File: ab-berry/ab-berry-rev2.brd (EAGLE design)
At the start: 58.4 x 61 mm, 72 parts, among them IC1 STM32F303CCT6, IC2 AT45DB161D-SU, U1 LM1117MPX-3.3/NOPB or AP2114H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, U2 PRTR5V0U2X

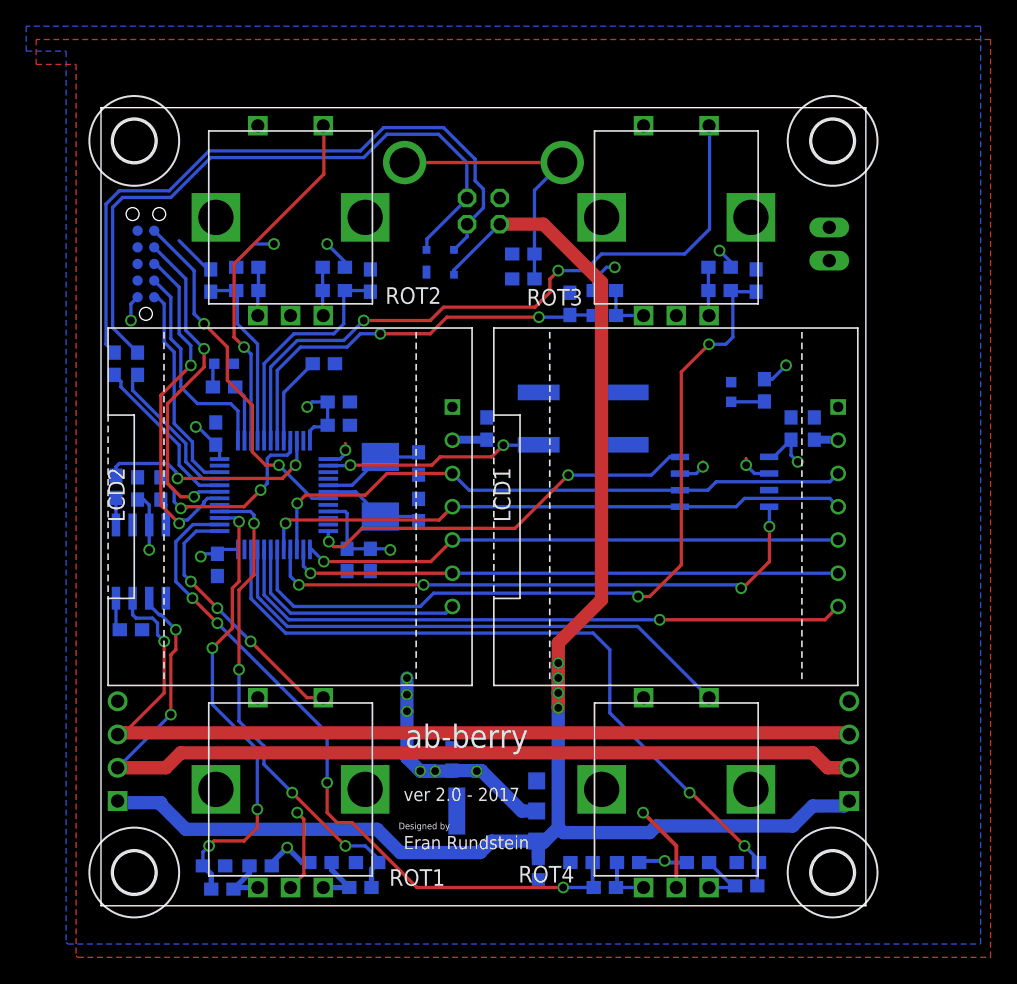
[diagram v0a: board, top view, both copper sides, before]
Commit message: make ab-berry-rev2 pass oshpask drc
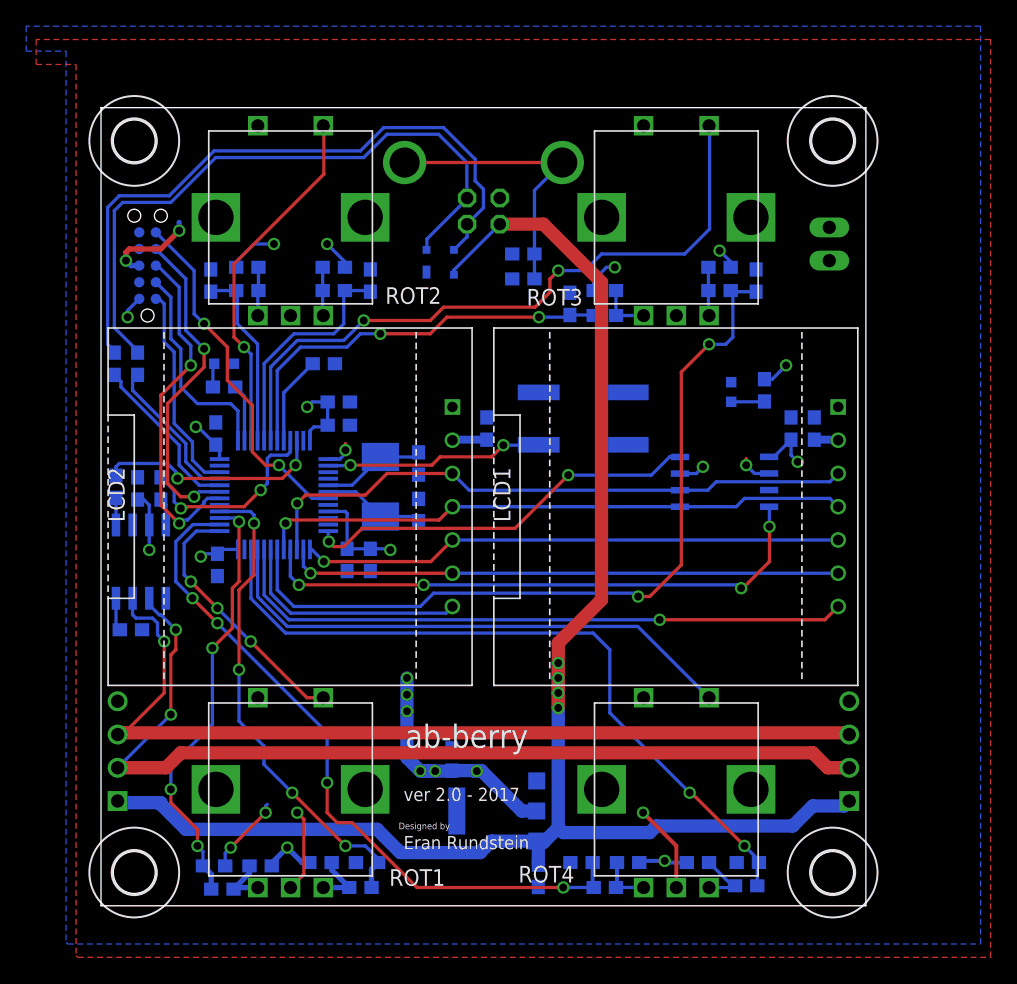
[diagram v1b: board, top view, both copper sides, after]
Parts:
- moved C8 0.51 mm to (33.4, 2.29)
- moved TC1 0.18 mm to (3.56, 48.9)
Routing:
- net GND: track 16.5 -> 26.3 mm, vias 2 -> 6
- net ROT1_A: track 35.3 -> 33.1 mm
- net 5.0V: track 122.2 -> 122.7 mm

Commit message: ab-berry-rev 2.1 wip
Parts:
- removed R2, R3, R4: 0, microbuilder:0603
- removed USR: (no value), microbuilder:EVQ-Q2
- added C24: 4.7nF, microbuilder:0603
- added CAN_TERM: (no value), pinhead+:2X02_SMT
- added R26, R27: 60 1%, microbuilder:0603
- D1: value SN65HVD232 -> SN65HVD230
- moved D1 1.65 mm to (2.97, 27.9)
- moved C3 0.92 mm to (9.40, 25.3)
- moved C7 0.80 mm to (3.05, 32.6), turned to 0 degrees
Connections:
- removed net BTN_USR: IC1.2, USR.B
- removed net N$2: D1.8, R2.1
- removed net N$4: D1.4, R3.1
- removed net N$5: D1.1, R4.1
- new net N$21: C24.2, D1.5, R26.2, R27.1
- new net N$22: CAN_TERM.2, R27.2
- new net N$23: CAN_TERM.4, R26.1
- net CAN_H: now also CAN_TERM.1
- net CAN_L: now also CAN_TERM.3
- net CAN_RX: now also D1.4; no longer R3.2
- net CAN_TX: now also D1.1; no longer R4.2
- net GND: now also C24.1, D1.8; no longer R2.2, USR.A
- net ROT1_A: now also IC1.25; no longer IC1.27
- net ROT1_B: now also IC1.26; no longer IC1.28
- net ROT1_SW: now also IC1.28; no longer IC1.25
- net ROT4_A: now also IC1.27; no longer IC1.26
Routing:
- net BTN_USR: track 16.7 -> 0.00 mm, vias 2 -> 0
- net N$21: track 0.00 -> 13.7 mm
- net CAN_H: track 69.3 -> 79.9 mm, vias 1 -> 2
- net CAN_L: track 72.8 -> 83.1 mm, vias 2 -> 3
- net N$2: track 2.53 -> 0.00 mm
- net N$22: track 0.00 -> 2.33 mm
- net N$23: track 0.00 -> 2.23 mm
- net ROT1_B: track 37.2 -> 35.0 mm
- net CAN_TX: track 17.5 -> 19.7 mm
- net N$4: track 2.10 -> 0.00 mm
- net N$5: track 2.07 -> 0.00 mm
- net CAN_RX: track 15.3 -> 13.5 mm
- net ROT4_A: track 54.4 -> 53.3 mm
- net 3.3V: track 85.1 -> 84.2 mm
- net ROT1_SW: track 20.0 -> 20.4 mm, vias 3 -> 1

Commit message: ab-berry rev2.1 sent to macrofab
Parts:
- removed CAN_TERM: (no value), pinhead+:2X02_SMT
- removed JP1, JP2: (no value), keves:1X04
- added TERM: (no value), pinhead:2X02
- added X2, X3: 04-JST-B4B-XH-A, bt_con-jst-xh:B4B-XH
- moved ROT1 43.7 mm to (14.5, 52.6)
- moved ROT2 43.7 mm to (14.5, 8.89)
- moved R27 5.75 mm to (6.60, 25.5), turned to 270 degrees
- moved C24 1.80 mm to (2.79, 21.5), turned to 180 degrees
- moved R26 1.80 mm to (2.79, 19.7)
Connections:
- removed net N$22: CAN_TERM.2, R27.2
- removed net N$23: CAN_TERM.4, R26.1
- new net N$4: R27.2, TERM.2
- new net N$5: R26.1, TERM.4
- net 5.0V: now also X2.P$1, X3.P$1; no longer JP1.1, JP2.1
- net CAN_H: now also TERM.1, X2.P$3, X3.P$3; no longer CAN_TERM.1, JP1.3, JP2.3
- net CAN_L: now also TERM.3, X2.P$2, X3.P$2; no longer CAN_TERM.3, JP1.2, JP2.2
- net GND: now also X2.P$4, X3.P$4; no longer JP1.4, JP2.4
- net N$10: now also ROT2.B; no longer ROT1.B
- net N$11: now also ROT2.A; no longer ROT1.A
- net N$14: now also ROT1.B; no longer ROT2.B
- net N$15: now also ROT1.A; no longer ROT2.A
- net ROT1_A: now also C18.1, IC1.40, R15.1; no longer C14.1, IC1.25, R7.1
- net ROT1_B: now also C19.1, IC1.41, R16.1; no longer C15.1, IC1.26, R8.1
- net ROT1_SW: now also IC1.39; no longer IC1.28
- net ROT2_A: now also C14.1, IC1.25, R7.1; no longer C18.1, IC1.40, R15.1
- net ROT2_B: now also C15.1, IC1.26, R8.1; no longer C19.1, IC1.41, R16.1
- net ROT2_SW: now also IC1.28; no longer IC1.39
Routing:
- net ROT2_A: track 14.1 -> 33.5 mm, vias 0 -> 4
- net ROT1_A: track 33.5 -> 14.1 mm, vias 4 -> 0
- net ROT2_B: track 17.8 -> 35.0 mm, vias 0 -> 4
- net ROT1_B: track 35.0 -> 17.8 mm, vias 4 -> 0
- net ROT2_SW: track 27.5 -> 20.4 mm
- net ROT1_SW: track 20.4 -> 27.5 mm
- net CAN_L: track 83.1 -> 76.5 mm, vias 3 -> 2
- net CAN_H: track 79.9 -> 74.5 mm, vias 2 -> 1
- net N$2: track 13.7 -> 10.3 mm
- net 5.0V: track 122.7 -> 119.7 mm
- net N$4: track 0.00 -> 2.51 mm
- net N$22: track 2.33 -> 0.00 mm
- net N$5: track 0.00 -> 2.30 mm
- net N$23: track 2.23 -> 0.00 mm
- net LCD_CS1: track 48.5 -> 47.6 mm
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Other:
- board text added: "+V"
- board text added: "GND"
- board text added: "H"
- board text added: "L"
- board text added: "ver 2.1 - 2017"
- board text removed: "ver 2.0 - 2017"
